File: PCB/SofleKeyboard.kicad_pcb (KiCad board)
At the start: 2 copper layers, 137.2 x 109.2 mm, 87 parts, among them J1 LED, J2 4PIN, J3 OLED, P1 i2c_pin, P2 i2c_pin, SW1 SW_PUSH, SW10 SW_PUSH, SW11 SW_PUSH, SW12 SW_PUSH, SW13 SW_PUSH, SW14 SW_PUSH, SW15 SW_PUSH, SW16 SW_PUSH, SW17 SW_PUSH, SW18 SW_PUSH, SW19 SW_PUSH, SW2 SW_PUSH, SW20 SW_PUSH, SW21 SW_PUSH, SW22 SW_PUSH, SW23 SW_PUSH, SW24 SW_PUSH, SW25 Rotary_Encoder_Switch, SW26 SW_PUSH, SW27 SW_PUSH, SW28 SW_PUSH, SW29 SW_PUSH, SW3 SW_PUSH, SW30 SW_PUSH, SW4 SW_PUSH, SW5 SW_PUSH, SW6 SW_PUSH, SW7 SW_PUSH, SW8 SW_PUSH, SW9 SW_PUSH, U1 ProMicro

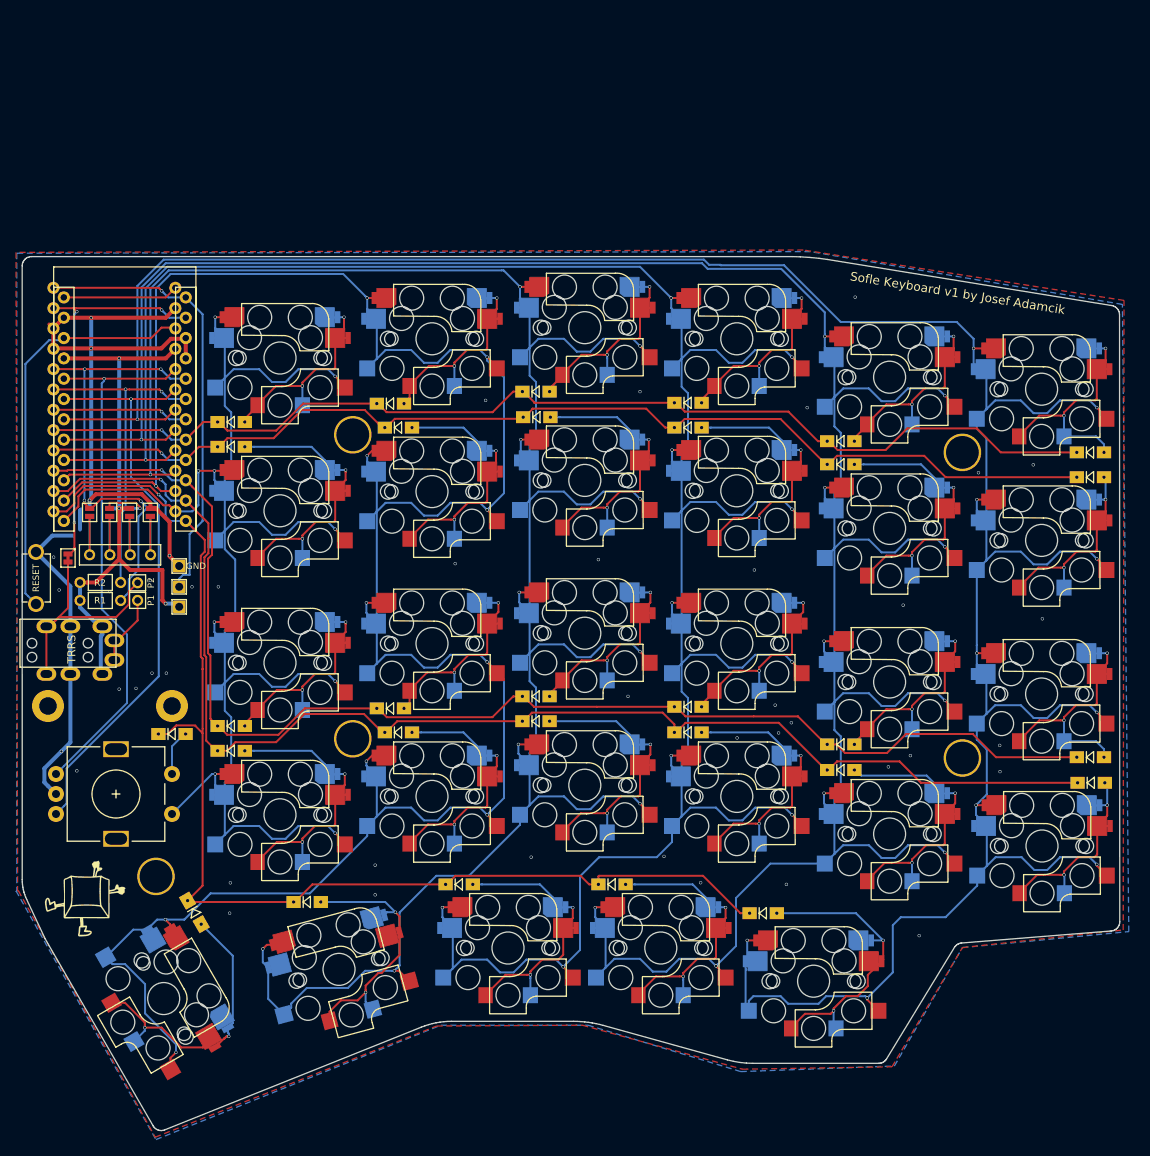
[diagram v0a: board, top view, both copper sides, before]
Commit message: footprints fixed, onto layout
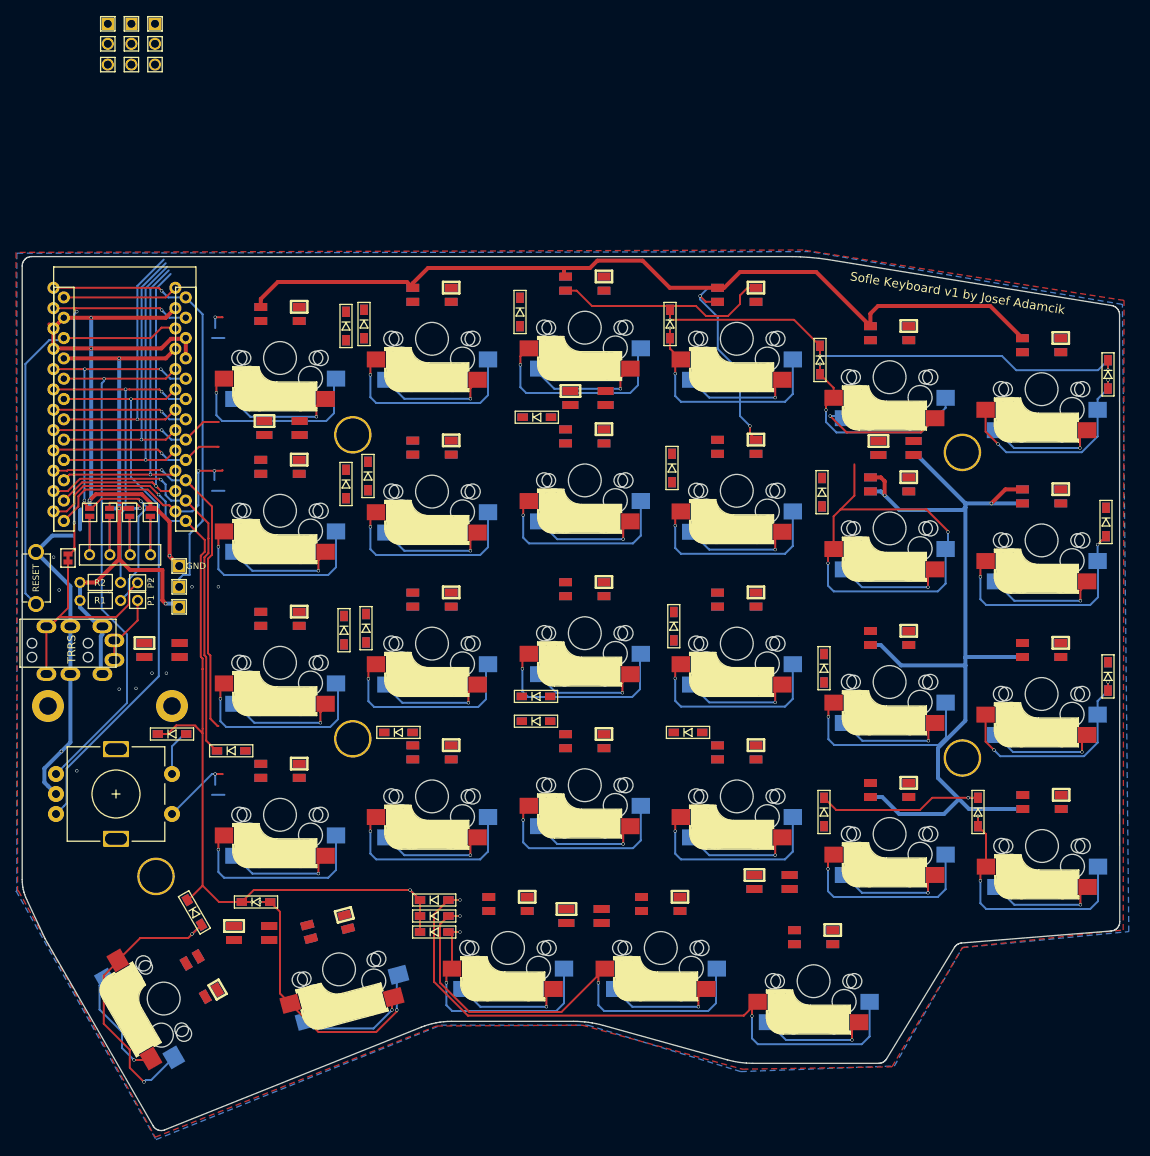
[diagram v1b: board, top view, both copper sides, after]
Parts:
- removed Ref** (x2): Val**, SofleKeyboard-footprint:SofleLogoSmall
- added D31: LED_sk2812_SM, LED_SMD:SK6812MINI_underglow_dev, F.Cu at (120.8, 58.8)
- added D32: LED_sk2812_SM, LED_SMD:SK6812MINI_underglow_dev, F.Cu at (159.0, 55.0)
- added D33: LED_sk2812_SM, LED_SMD:SK6812MINI_underglow_dev, F.Cu at (197.5, 61.2)
- added D34: LED_sk2812_SM, LED_SMD:SK6812MINI_underglow_dev, F.Cu at (117.0, 121.9)
- added D35: LED_sk2812_SM, LED_SMD:SK6812MINI_underglow_dev, F.Cu at (158.5, 119.8)
- added D36: LED_sk2812_SM, LED_SMD:SK6812MINI_underglow_dev, F.Cu at (182.0, 115.5)
- added D37: LED_sk2812_SM, LED_SMD:SK6812MINI_underglow_dev, F.Cu at (105.8, 86.5)
- added J4: key leds, Connector:3x1header, F.Cu at (99.0, 8.23)
- added J5: backlight sel, Connector:3x1header, F.Cu at (101.9, 8.23)
- added J6: indicator bypass, Connector:3x1header, F.Cu at (104.9, 8.23)
- D1, D10, D11, D12, D13, D14, D15, D16, D17, D18, D19, D2, D20, D21, D22, D23, D24, D25, D26, D27, D28, D29, D3, D30, D4, D5, D6, D7, D8, D9: footprint SofleKeyboard-footprint:Diode_SOD123 -> Diode_SMD:crkbd-diode
- SW1, SW10, SW11, SW12, SW13, SW14, SW15, SW16, SW17, SW18, SW19, SW2, SW20, SW21, SW22, SW23, SW24, SW27, SW28, SW29, SW3, SW30, SW4, SW5, SW6, SW7, SW8, SW9: value SW_PUSH -> SW_PUSH-MX_W_LED; footprint SofleKeyboard-footprint:CherryMX_KailhLowProfile_Hotswap -> Button_Switch_Keyboard:SK6812MINI_and_cherry
- SW26: value SW_PUSH -> SW_PUSH-MX_W_LED; footprint SofleKeyboard-footprint:CherryMX_KailhLowProfile_Hotswap_1.5 -> Button_Switch_Keyboard:SK6812MINI_and_cherry
- moved D30 41.2 mm to (139.8, 117.8)
- moved D29 22.6 mm to (139.8, 119.8)
- moved D1 18.7 mm to (128.8, 46.0), turned to 270 degrees
- moved D13 18.5 mm to (128.5, 84.0), turned to 270 degrees
- moved D7 15.1 mm to (128.8, 65.8), turned to 270 degrees
- moved D24 14.6 mm to (207.8, 106.8), turned to 270 degrees
- moved D2 10.5 mm to (131.0, 45.8), turned to 270 degrees
- moved D14 10.5 mm to (131.2, 83.8), turned to 270 degrees
- moved D5 10.5 mm to (188.0, 50.2), turned to 270 degrees
- moved D18 10.3 mm to (224.0, 89.8), turned to 270 degrees
- moved D16 10.2 mm to (169.7, 83.5), turned to 270 degrees
- moved D3 10.1 mm to (150.5, 44.2), turned to 270 degrees
- moved D4 10.1 mm to (169.2, 45.8), turned to 270 degrees
- moved D6 10.00 mm to (224.0, 52.0), turned to 270 degrees
- moved D17 9.75 mm to (188.5, 88.8), turned to 270 degrees
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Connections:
- SW1 pad 1: SW25A -> Net-(SW1-Pad1)
- SW1 pad 2: Net-(D1-Pad2) -> GND
- SW10 pad 1: col2 -> Net-(SW10-Pad1)
- SW10 pad 2: Net-(D10-Pad2) -> GND
- SW11 pad 1: col1 -> Net-(SW11-Pad1)
- SW11 pad 2: Net-(D11-Pad2) -> GND
- SW12 pad 1: col0 -> Net-(SW12-Pad1)
- SW12 pad 2: Net-(D12-Pad2) -> GND
- SW13 pad 1: SW25A -> Net-(SW13-Pad1)
- SW13 pad 2: Net-(D13-Pad2) -> GND
- SW14 pad 1: col4 -> Net-(SW14-Pad1)
- SW14 pad 2: Net-(D14-Pad2) -> GND
- SW15 pad 1: col3 -> Net-(SW15-Pad1)
- SW15 pad 2: Net-(D15-Pad2) -> GND
- SW16 pad 1: col2 -> Net-(SW10-Pad3)
- SW16 pad 2: Net-(D16-Pad2) -> GND
- SW17 pad 1: col1 -> Net-(SW17-Pad1)
- SW17 pad 2: Net-(D17-Pad2) -> GND
- SW18 pad 1: col0 -> Net-(SW12-Pad3)
- SW18 pad 2: Net-(D18-Pad2) -> GND
- SW19 pad 1: SW25A -> Net-(SW19-Pad1)
- SW19 pad 2: Net-(D19-Pad2) -> GND
- SW2 pad 1: col4 -> Net-(SW1-Pad3)
- SW2 pad 2: Net-(D2-Pad2) -> GND
- SW20 pad 1: col4 -> Net-(SW14-Pad3)
- SW20 pad 2: Net-(D20-Pad2) -> GND
- SW21 pad 1: col3 -> Net-(SW21-Pad1)
- SW21 pad 2: Net-(D21-Pad2) -> GND
- SW22 pad 1: col2 -> Net-(SW16-Pad3)
- SW22 pad 2: Net-(D22-Pad2) -> GND
- SW23 pad 1: col1 -> Net-(SW23-Pad1)
- SW23 pad 2: Net-(D23-Pad2) -> GND
- SW24 pad 1: col0 -> Net-(SW18-Pad3)
- SW24 pad 2: Net-(D24-Pad2) -> GND
- SW26 pad 1: col4 -> Net-(SW20-Pad3)
- SW26 pad 2: Net-(D26-Pad2) -> GND
- SW27 pad 1: col3 -> Net-(SW26-Pad3)
- SW27 pad 2: Net-(D27-Pad2) -> GND
- SW28 pad 1: col2 -> Net-(SW22-Pad3)
- SW28 pad 2: Net-(D28-Pad2) -> GND
- SW29 pad 1: col1 -> Net-(SW28-Pad3)
- SW29 pad 2: Net-(D29-Pad2) -> GND
- SW3 pad 1: col3 -> Net-(SW3-Pad1)
- SW3 pad 2: Net-(D3-Pad2) -> GND
- SW30 pad 1: col0 -> Net-(SW24-Pad3)
- SW30 pad 2: Net-(D30-Pad2) -> GND
- SW4 pad 1: col2 -> Net-(SW3-Pad3)
- SW4 pad 2: Net-(D4-Pad2) -> GND
- SW5 pad 1: col1 -> Net-(SW11-Pad3)
- SW5 pad 2: Net-(D5-Pad2) -> GND
- SW6 pad 1: col0 -> Net-(SW5-Pad3)
- SW6 pad 2: Net-(D6-Pad2) -> GND
- SW7 pad 1: SW25A -> Net-(SW13-Pad3)
- SW7 pad 2: Net-(D7-Pad2) -> GND
- SW8 pad 1: col4 -> Net-(SW2-Pad3)
- SW8 pad 2: Net-(D8-Pad2) -> GND
- SW9 pad 1: col3 -> Net-(SW15-Pad3)
- SW9 pad 2: Net-(D9-Pad2) -> GND
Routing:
- net col0: track 358.0 -> 106.0 mm, vias 11 -> 6
- net col1: track 350.6 -> 111.7 mm, vias 11 -> 6
- net VCC: track 74.2 -> 301.3 mm, vias 3 -> 5
- net col2: track 334.4 -> 109.8 mm, vias 11 -> 6
- net col3: track 314.7 -> 110.9 mm, vias 11 -> 6
- net col4: track 311.0 -> 113.0 mm, vias 11 -> 6
- net row1: track 138.3 -> 21.9 mm
- net row2: track 165.8 -> 50.0 mm
- net SW25A: track 206.1 -> 97.3 mm, vias 9 -> 8
- net row3: track 170.1 -> 74.3 mm, vias 1 -> 2
- net row0: track 138.2 -> 87.0 mm, vias 1 -> 4
- net Net-(D30-Pad2): track 37.0 -> 81.4 mm
- net row4: track 152.5 -> 118.8 mm, vias 1 -> 3
- net Net-(SW3-Pad3): track 0.00 -> 27.4 mm
- net Net-(D1-Pad2): track 27.9 -> 1.56 mm, vias 2 -> 0
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
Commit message: layout done. need schematic, footprint and pcb review
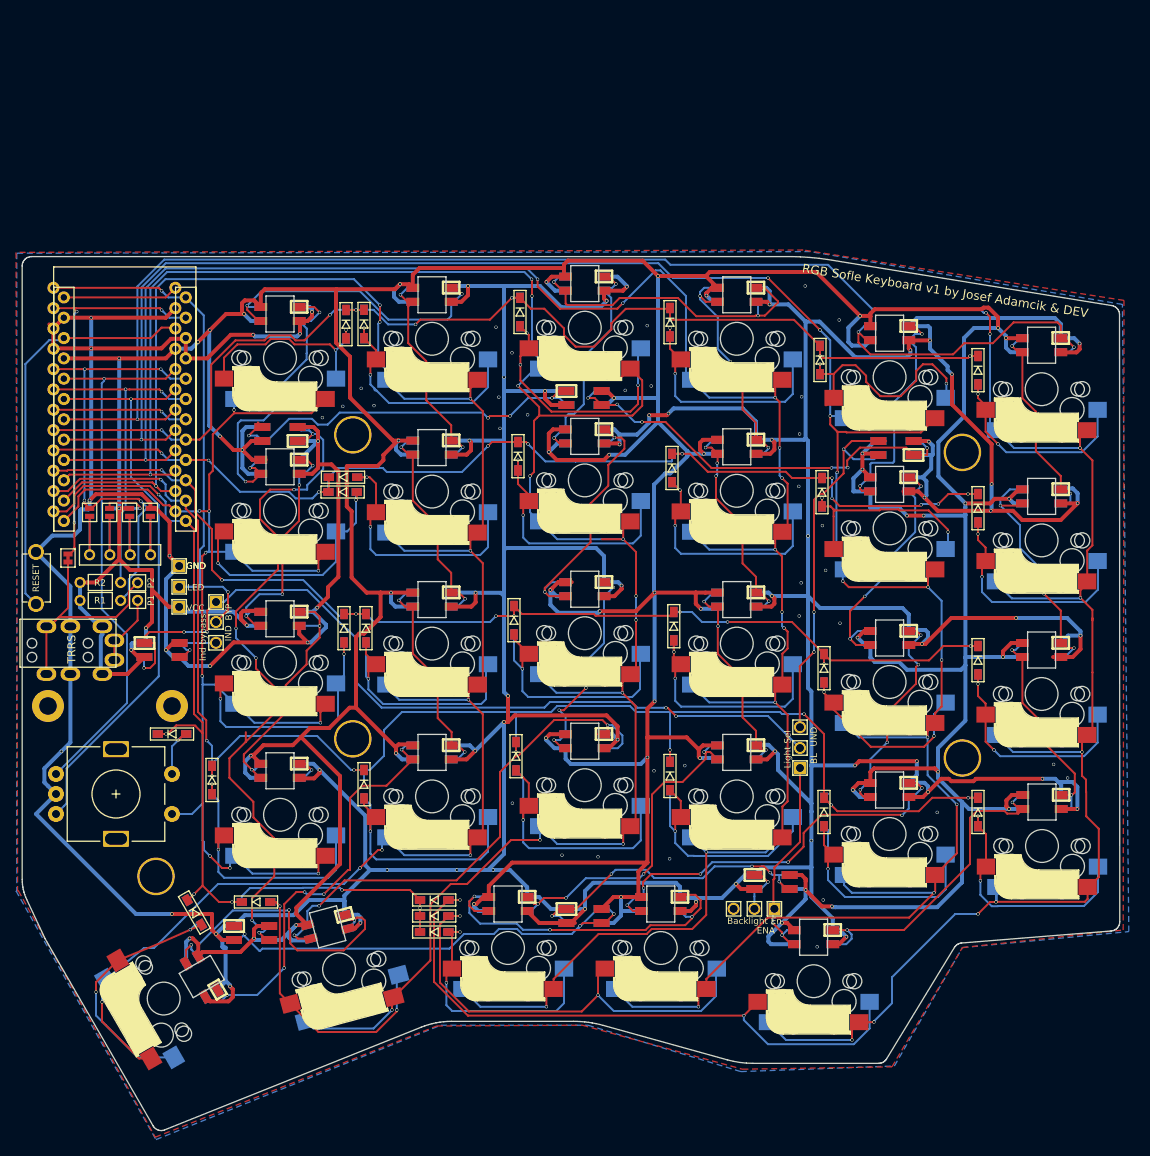
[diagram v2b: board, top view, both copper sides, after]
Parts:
- moved J5 136.7 mm to (182.3, 118.8), turned to 270 degrees
- moved J4 127.0 mm to (185.5, 101.2), turned to 180 degrees
- moved J6 72.7 mm to (112.5, 80.5)
- moved D18 16.4 mm to (207.8, 87.8)
- moved D6 16.3 mm to (207.8, 51.5)
- moved D12 16.1 mm to (207.8, 68.8)
- moved D15 9.91 mm to (149.8, 82.8), turned to 270 degrees
- moved D20 7.77 mm to (131.0, 103.3), turned to 270 degrees
- moved D22 5.90 mm to (169.2, 102.2), turned to 270 degrees
- moved D9 5.41 mm to (150.2, 62.3), turned to 270 degrees
- moved D21 5.04 mm to (150.0, 99.8), turned to 270 degrees
- moved D19 4.37 mm to (112.0, 102.8), turned to 270 degrees
- moved D8 3.13 mm to (128.4, 64.9), turned to 0 degrees
- moved D7 1.09 mm to (128.3, 66.8), turned to 0 degrees
- moved D31 0.79 mm to (120.5, 59.5), turned to 180 degrees
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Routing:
- net GND: track 124.4 -> 987.2 mm, vias 16 -> 94
- net VCC: track 301.3 -> 911.1 mm, vias 5 -> 52
- net col0: track 106.0 -> 311.1 mm, vias 6 -> 10
- net col1: track 111.7 -> 300.1 mm, vias 6 -> 12
- net col2: track 109.8 -> 275.2 mm, vias 6 -> 13
- net col3: track 110.9 -> 267.0 mm, vias 6 -> 12
- net col4: track 113.0 -> 245.1 mm, vias 6 -> 10
- net row3: track 74.3 -> 191.0 mm, vias 2 -> 9
- net row1: track 21.9 -> 137.7 mm, vias 1 -> 11
- net lights: track 0.00 -> 105.5 mm, vias 0 -> 5
- net row2: track 50.0 -> 142.0 mm, vias 1 -> 9
- net Net-(D31-Pad1): track 0.00 -> 91.6 mm, vias 0 -> 6
- net Net-(SW21-Pad1): track 0.00 -> 66.6 mm, vias 0 -> 3
- net row0: track 87.0 -> 147.2 mm, vias 4 -> 8
- net Net-(D34-Pad1): track 0.00 -> 59.0 mm, vias 0 -> 3
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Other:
- outline, holes or cut-outs redrawn
- board text added: "BL"
- board text added: "BYP"
- board text added: "Backlight En"
- board text added: "ENA"
- board text added: "IND"
- board text added: "Ind bypass"
- board text added: "LED"
- board text added: "Light Sel"
- board text added: "RGB Sofle Keyboard v1 by Josef Adamcik & DEV"
- board text added: "UND"
- board text added: "VCC"
- board text removed: "Sofle Keyboard v1 by Josef Adamcik"
